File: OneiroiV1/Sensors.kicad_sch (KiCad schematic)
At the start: 19 parts, among them J5 3-1478978-1, U1 LSM6DSV80XTR, U15 H3LIS331DLTR, U18 MS561101BA03-50, U19 MS561101BA03-50, U2 MAX-M10S-00B, U20 BMI323, U21 BMI270

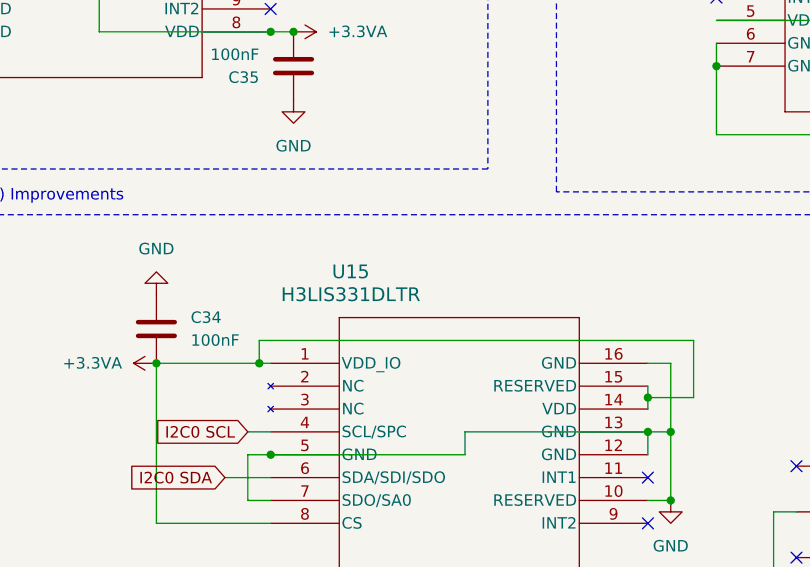
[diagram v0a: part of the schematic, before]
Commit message: Oneiroi Changes
All 3D models and footprints updated to common library, silkscreening must be re-done.
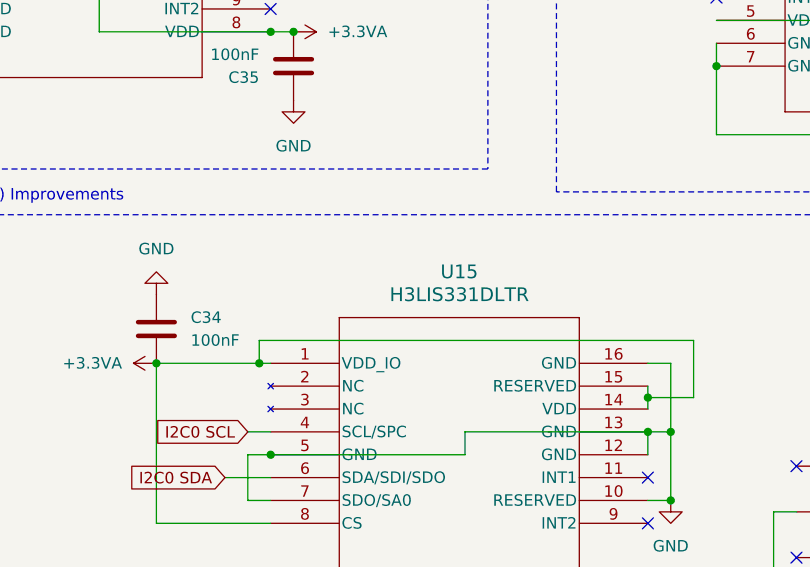
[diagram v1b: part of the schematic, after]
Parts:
- A2: footprint Baro 1:XDCR_LPS22DFTR -> UNSW Rocketry Library:XDCR_LPS22DFTR; symbol Barometer:LPS22DFTR -> UNSW Rocketry Library:LPS22DFTR
- J5: footprint SMA right angle:TE_3-1478978-1 -> UNSW Rocketry Library:TE_3-1478978-1; symbol SMA right angle:3-1478978-1 -> UNSW Rocketry Library:3-1478978-1
- U1: footprint Acc 1:QFN_LSM6DSV80XTR_STM -> UNSW Rocketry Library:QFN_LSM6DSV80XTR_STM; symbol IMU:LSM6DSV80XTR -> UNSW Rocketry Library:LSM6DSV80XTR
- U15: footprint high-g acc:QFN_31DLTR_STM -> UNSW Rocketry Library:QFN_31DLTR_STM; symbol High-G acc:H3LIS331DLTR -> UNSW Rocketry Library:H3LIS331DLTR
- U18, U19: footprint ms5611:SON8_MS5611_TEC -> UNSW Rocketry Library:SON8_MS5611_TEC; symbol high-alt Baro:MS561101BA03-50 -> UNSW Rocketry Library:MS561101BA03-50
- U2: footprint GPS:XCVR_MAX-M10S-00B -> UNSW Rocketry Library:XCVR_MAX-M10S-00B; symbol GPS Module:MAX-M10S-00B -> UNSW Rocketry Library:MAX-M10S-00B
- U20: footprint BMI323:BMI323_BOS -> UNSW Rocketry Library:BMI323_BOS; symbol 16g acc:BMI323 -> UNSW Rocketry Library:BMI323
- U21: footprint BMI270:BMI270_BOS -> UNSW Rocketry Library:BMI270_BOS; symbol alt 16g acc:BMI270 -> UNSW Rocketry Library:BMI270
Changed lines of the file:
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@@
 	)
 	(symbol
-		(lib_id "High-G acc:H3LIS331DLTR")
+		(lib_id "UNSW Rocketry Library:H3LIS331DLTR")
 		(at 138.43 119.38 0)
 		(unit 1)
@@
 		(fields_autoplaced yes)
 		(property "Reference" "U15"
-			(at 171.45 109.22 0)
+			(at 183.515 109.22 0)
 			(show_name no)
 			(do_not_autoplace no)
@@
 		)
 		(property "Value" "H3LIS331DLTR"
-			(at 171.45 111.76 0)
+			(at 183.515 111.76 0)
 			(show_name no)
 			(do_not_autoplace no)
@@
 			)
 		)
-		(property "Footprint" "high-g acc:QFN_31DLTR_STM"
-			(at 138.43 119.38 0)
+		(property "Footprint" "UNSW Rocketry Library:QFN_31DLTR_STM"
+			(at 162.56 119.38 0)
 			(hide yes)
 			(show_name no)
@@
 		)
 		(property "Datasheet" "https://www.st.com/resource/en/datasheet/h3lis331dl.pdf"
-			(at 138.43 119.38 0)
+			(at 162.56 119.38 0)
 			(hide yes)
 			(show_name no)
@@
 	)
 	(symbol
-		(lib_id "high-alt Baro:MS561101BA03-50")
+		(lib_id "UNSW Rocketry Library:MS561101BA03-50")
 		(at 228.6 44.45 0)
 		(unit 1)
@@
 			)
 		)
-		(property "Footprint" "ms5611:SON8_MS5611_TEC"
+		(property "Footprint" "UNSW Rocketry Library:SON8_MS5611_TEC"
 			(at 228.6 44.45 0)
 			(hide yes)
@@
 	)
 	(symbol
-		(lib_id "16g acc:BMI323")
+		(lib_id "UNSW Rocketry Library:BMI323")
 		(at 212.09 71.12 0)
 		(unit 1)
@@
 			)
 		)
-		(property "Footprint" "BMI323:BMI323_BOS"
+		(property "Footprint" "UNSW Rocketry Library:BMI323_BOS"
 			(at 212.09 71.12 0)
 			(hide yes)
@@
 	)
 	(symbol
-		(lib_id "Barometer:LPS22DFTR")
+		(lib_id "UNSW Rocketry Library:LPS22DFTR")
 		(at 44.45 45.72 0)
 		(unit 1)
@@
 			)
 		)
-		(property "Footprint" "Baro 1:XDCR_LPS22DFTR"
+		(property "Footprint" "UNSW Rocketry Library:XDCR_LPS22DFTR"
 			(at 44.45 45.72 0)
 			(hide yes)
@@
 	)
 	(symbol
-		(lib_id "SMA right angle:3-1478978-1")
+		(lib_id "UNSW Rocketry Library:3-1478978-1")
 		(at 226.06 176.53 0)
 		(unit 1)
@@
 			)
 		)
-		(property "Footprint" "SMA right angle:TE_3-1478978-1"
+		(property "Footprint" "UNSW Rocketry Library:TE_3-1478978-1"
 			(at 226.06 176.53 0)
 			(hide yes)
@@
 	)
 	(symbol
-		(lib_id "alt 16g acc:BMI270")
+		(lib_id "UNSW Rocketry Library:BMI270")
 		(at 31.75 80.01 0)
 		(unit 1)
@@
 			)
 		)
-		(property "Footprint" "BMI270:BMI270_BOS"
+		(property "Footprint" "UNSW Rocketry Library:BMI270_BOS"
 			(at 31.75 80.01 0)
 			(hide yes)
@@
 	)
 	(symbol
-		(lib_id "IMU:LSM6DSV80XTR")
+		(lib_id "UNSW Rocketry Library:LSM6DSV80XTR")
 		(at 121.92 67.31 0)
 		(unit 1)
@@
 			)
 		)
-		(property "Footprint" "Acc 1:QFN_LSM6DSV80XTR_STM"
-			(at 121.92 67.31 0)
+		(property "Footprint" "UNSW Rocketry Library:QFN_LSM6DSV80XTR_STM"
+			(at 122.682 55.372 0)
 			(hide yes)
 			(show_name no)
@@
 		)
 		(property "Datasheet" "https://www.st.com/resource/en/datasheet/lsm6dsv80x.pdf"
-			(at 121.92 67.31 0)
+			(at 121.412 51.308 0)
 			(hide yes)
 			(show_name no)
@@
 	)
 	(symbol
-		(lib_id "high-alt Baro:MS561101BA03-50")
+		(lib_id "UNSW Rocketry Library:MS561101BA03-50")
 		(at 139.7 43.18 0)
 		(unit 1)
@@
 			)
 		)
-		(property "Footprint" "ms5611:SON8_MS5611_TEC"
+		(property "Footprint" "UNSW Rocketry Library:SON8_MS5611_TEC"
 			(at 139.7 43.18 0)
 			(hide yes)
@@
 	)
 	(symbol
-		(lib_id "GPS Module:MAX-M10S-00B")
+		(lib_id "UNSW Rocketry Library:MAX-M10S-00B")
 		(at 243.84 135.89 0)
 		(unit 1)
@@
 			)
 		)
-		(property "Footprint" "GPS:XCVR_MAX-M10S-00B"
+		(property "Footprint" "UNSW Rocketry Library:XCVR_MAX-M10S-00B"
 			(at 243.84 135.89 0)
 			(hide yes)
